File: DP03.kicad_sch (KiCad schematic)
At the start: 2 parts

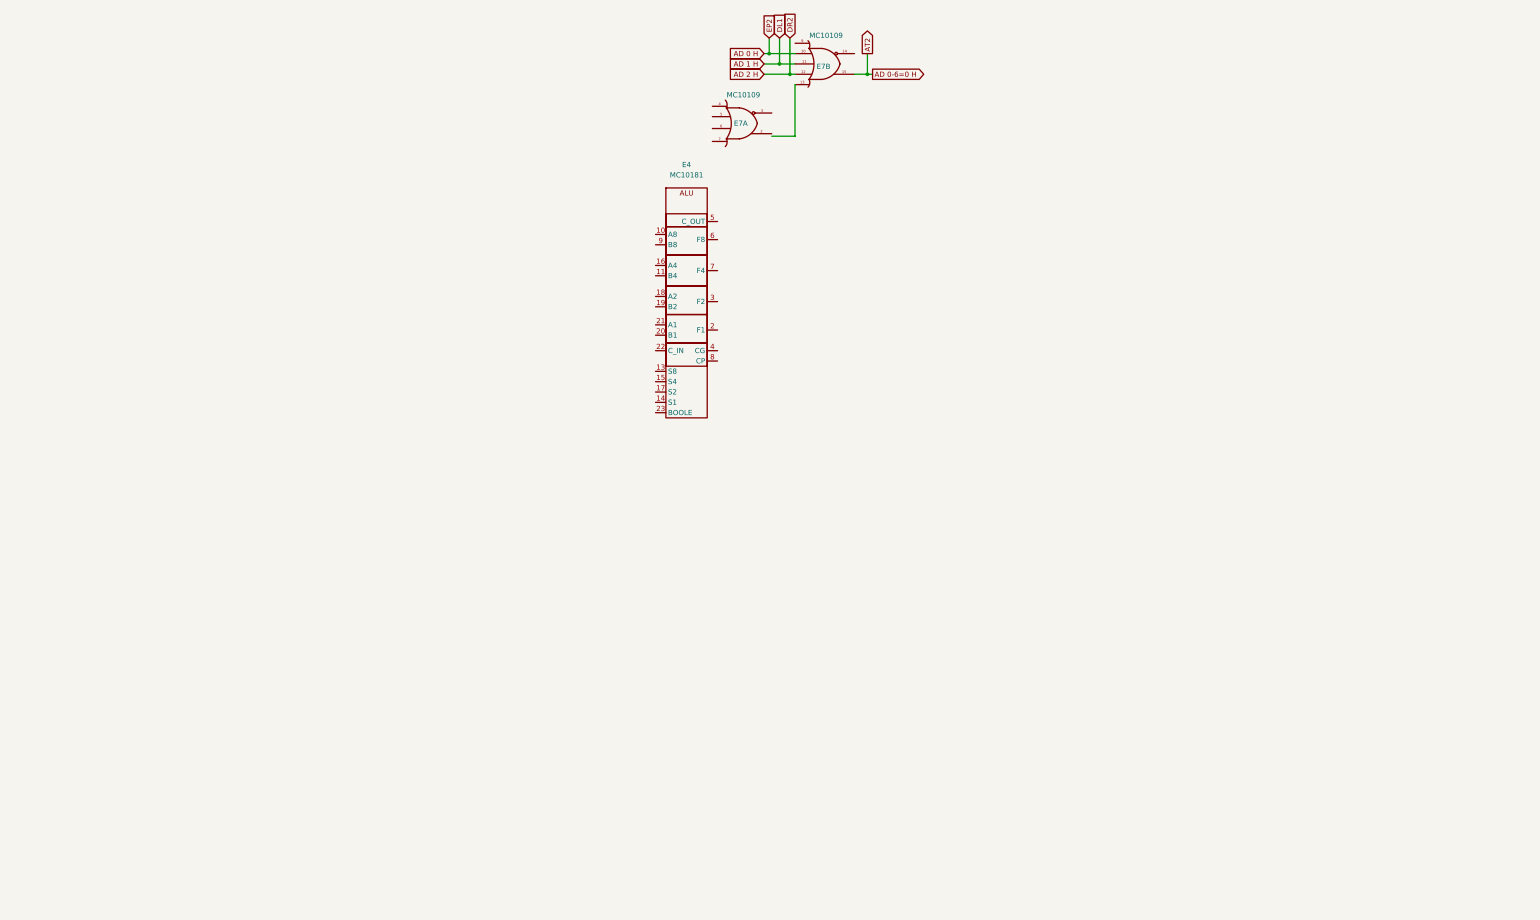
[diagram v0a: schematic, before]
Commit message: EDP is "done" but there is still much work to do to standardize and set up netlist export and verilog creation
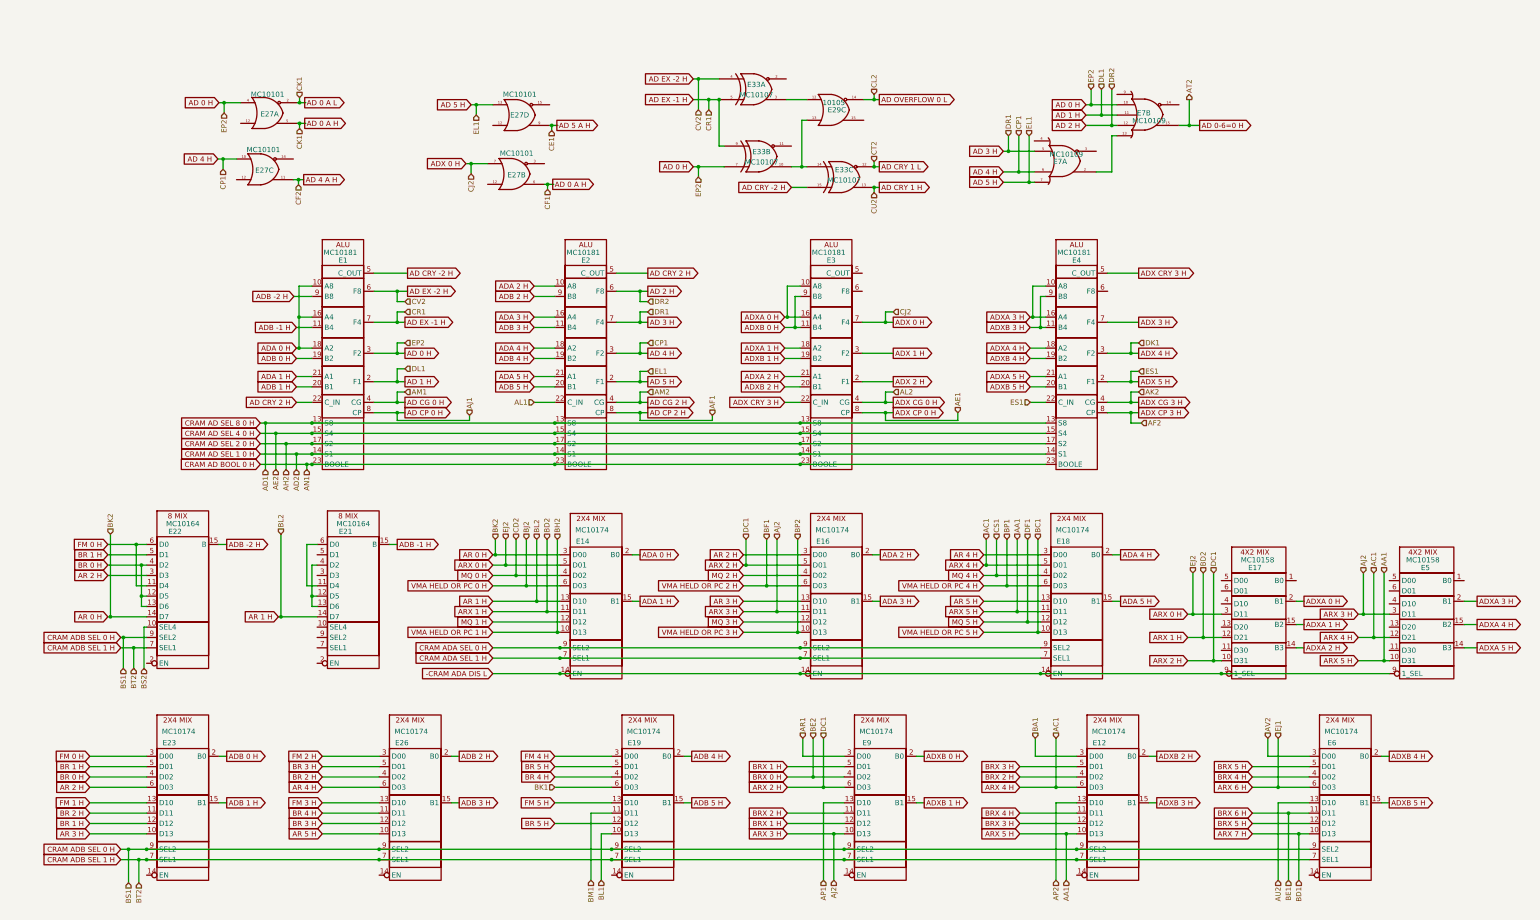
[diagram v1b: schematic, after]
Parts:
- added E1, E2, E3: MC10181, symbol DEC20:MC10181
- added E12, E14, E16, E18, E19, E23, E26, E6, E9: MC10174, symbol DEC20:MC10174
- added E17, E5: MC10158, symbol DEC20:MC10158
- added E21, E22: MC10164, symbol DEC20:MC10164
- added E27: MC10101, symbol DEC20:MC10101
- added E29: 10105, symbol DEC20:MC10105
- added E33: MC10107, symbol DEC20:MC10107
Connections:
- net AD 0 H: now also E1.3 (F2), E27.4 (Ain), E33.7 (Bin2)
- net AD 1 H: now also E1.2 (F1)
- net AD 2 H: now also E2.6 (F8)
- net GEE: now also E1.12 (GEE), E2.12 (GEE), E3.12 (GEE)
- net VCC1: now also E1.1 (VCC1), E12.1 (VCC1), E14.1 (VCC1), E16.1 (VCC1), E17.1 (VCC1), E18.1 (VCC1), E19.1 (VCC1), E2.1 (VCC1), E21.1 (VCC1), E22.1 (VCC1), E23.1 (VCC1), E26.1 (VCC1), E27.1 (VCC1), E27.1 (VCC1), E27.1 (VCC1), E27.1 (VCC1), E29.1 (VCC1), E3.1 (VCC1), E33.1 (VCC1), E33.1 (VCC1), E33.1 (VCC1), E5.1 (VCC1), E6.1 (VCC1), E9.1 (VCC1)
- net VCC2: now also E1.24 (VCC2), E12.16 (VCC2), E14.16 (VCC2), E16.16 (VCC2), E17.16 (VCC2), E18.16 (VCC2), E19.16 (VCC2), E2.24 (VCC2), E21.16 (VCC2), E22.16 (VCC2), E23.16 (VCC2), E26.16 (VCC2), E27.16 (VCC2), E27.16 (VCC2), E27.16 (VCC2), E27.16 (VCC2), E29.16 (VCC2), E3.24 (VCC2), E33.16 (VCC2), E33.16 (VCC2), E33.16 (VCC2), E5.16 (VCC2), E6.16 (VCC2), E9.16 (VCC2)
- net ADXA 3 H: now reaches E4.10 (A8)
- net ADXA 3 H: now also E4.16 (A4), E5.2 (B1)
- net ADXB 3 H: now reaches E4.11 (B4)
- net ADXB 3 H: now also E4.9 (B8), E12.15 (B1)
- net CRAM AD SEL 8 0 H: now reaches E4.13 (S8)
- net CRAM AD SEL 8 0 H: now also E1.13 (S8), E2.13 (S8), E3.13 (S8)
- net CRAM AD SEL 1 0 H: now reaches E4.14 (S1)
- net CRAM AD SEL 1 0 H: now also E1.14 (S1), E2.14 (S1), E3.14 (S1)
- net CRAM AD SEL 4 0 H: now reaches E4.15 (S4)
- net CRAM AD SEL 4 0 H: now also E1.15 (S4), E2.15 (S4), E3.15 (S4)
- net CRAM AD SEL 2 0 H: now reaches E4.17 (S2)
- net CRAM AD SEL 2 0 H: now also E1.17 (S2), E2.17 (S2), E3.17 (S2)
- net ADXA 4 H: now reaches E4.18 (A2)
- net ADXA 4 H: now also E5.15 (B2)
- net ADXB 4 H: now reaches E4.19 (B2)
- net ADXB 4 H: now also E6.2 (B0)
- net ADX 5 H: now reaches E4.2 (F1)
- net ADX 5 H: now also E4.22 (C_IN)
- net ADXB 5 H: now reaches E4.20 (B1)
- net ADXB 5 H: now also E6.15 (B1)
- net ADXA 5 H: now reaches E4.21 (A1)
- net ADXA 5 H: now also E5.14 (B3)
- net CRAM AD BOOL 0 H: now reaches E4.23 (BOOLE)
- net CRAM AD BOOL 0 H: now also E1.23 (BOOLE), E2.23 (BOOLE), E3.23 (BOOLE)
- net ADX 4 H: now reaches E4.3 (F2)
- net ADX CG 3 H: now reaches E4.4 (CG)
- net ADX CRY 3 H: now reaches E4.5 (C_OUT)
- net ADX CRY 3 H: now also E3.22 (C_IN)
- net ADX 3 H: now reaches E4.7 (F4)
- net ADX CP 3 H: now reaches E4.8 (CP)
- net at E7.2 (Aout): now also E7.13 (Bin5)
- net AD 3 H: now reaches E7.5 (Bin2)
- net AD 3 H: now also E2.7 (F4)
- net AD 4 H: now reaches E7.6 (Bin3)
- net AD 4 H: now also E2.3 (F2), E27.10 (Cin)
- net AD 5 H: now reaches E7.7 (Bin4)
- net AD 5 H: now also E2.2 (F1), E27.13 (Din)
- new net: E29.12 (Cin1), E33.3 (Aout)
- new net: E29.13 (Cin2), E33.10 (Bout), E33.14 (Cin1)
- new net: E21.11 (D4), E21.6 (D0)
- new net: E21.12 (D5), E21.13 (D6), E21.4 (D2)
- new net -CRAM ADA DIS L: E14.14 (EN), E16.14 (EN), E17.9 (1_SEL), E18.14 (EN), E5.9 (1_SEL)
- new net AD 0 A H: E27.2 (~Aout), E27.5 (Aout), E27.6 (Bout)
- new net AD 4 A H: E27.11 (Cout)
- new net AD 5 A H: E27.9 (Dout)
- new net AD CG 0 H: E1.4 (CG)
- new net AD CG 2 H: E2.4 (CG)
- new net AD CP 0 H: E1.8 (CP)
- new net AD CP 2 H: E2.8 (CP)
- new net AD CRY -2 H: E1.5 (C_OUT), E33.15 (Cin2)
- new net AD CRY 1 H: E33.13 (Cout)
- new net AD CRY 1 L: E33.12 (~Cout)
- new net AD CRY 2 H: E1.22 (C_IN), E2.5 (C_OUT)
- new net AD EX -1 H: E1.7 (F4), E33.5 (Ain2), E33.9 (Bin1)
- new net AD EX -2 H: E1.6 (F8), E33.4 (Ain1)
- new net AD OVERFLOW 0 L: E29.14 (~Cout)
- new net ADA 0 H: E1.10 (A8), E1.16 (A4), E1.18 (A2), E14.2 (B0)
- new net ADA 1 H: E1.21 (A1), E14.15 (B1)
- new net ADA 2 H: E16.2 (B0), E2.10 (A8)
- new net ADA 3 H: E16.15 (B1), E2.16 (A4)
- new net ADA 4 H: E18.2 (B0), E2.18 (A2)
- new net ADA 5 H: E18.15 (B1), E2.21 (A1)
- new net ADB -1 H: E1.11 (B4), E21.15 (B)
- new net ADB -2 H: E1.9 (B8), E22.15 (B)
- new net ADB 0 H: E1.19 (B2), E23.2 (B0)
- new net ADB 1 H: E1.20 (B1), E23.15 (B1)
- new net ADB 2 H: E2.9 (B8), E26.2 (B0)
- new net ADB 3 H: E2.11 (B4), E26.15 (B1)
- new net ADB 4 H: E19.2 (B0), E2.19 (B2)
- new net ADB 5 H: E19.15 (B1), E2.20 (B1)
- new net ADX 0 H: E27.7 (Bin), E3.7 (F4)
- new net ADX 1 H: E3.3 (F2)
- new net ADX 2 H: E3.2 (F1)
- new net ADX CG 0 H: E3.4 (CG)
- new net ADX CP 0 H: E3.8 (CP)
- new net ADXA 0 H: E17.2 (B1), E3.10 (A8), E3.16 (A4)
- new net ADXA 1 H: E17.15 (B2), E3.18 (A2)
- new net ADXA 2 H: E17.14 (B3), E3.21 (A1)
- new net ADXB 0 H: E3.11 (B4), E3.9 (B8), E9.2 (B0)
- new net ADXB 1 H: E3.19 (B2), E9.15 (B1)
- new net ADXB 2 H: E12.2 (B0), E3.20 (B1)
- new net AL1: E2.22 (C_IN)
- new net AP1: E9.13 (D10)
- new net AP2: E12.13 (D10)
- new net AR 0 H: E14.3 (D00), E22.14 (D7)
- new net AR 1 H: E14.13 (D10), E21.14 (D7)
- new net AR 2 H: E16.3 (D00), E22.3 (D3), E23.6 (D03)
- new net AR 3 H: E16.13 (D10), E23.10 (D13)
- new net AR 4 H: E18.3 (D00), E26.6 (D03)
- new net AR 5 H: E18.13 (D10), E26.10 (D13)
- new net AR1: E9.3 (D00)
- new net ARX 0 H: E14.5 (D01), E17.3 (D11)
- new net ARX 1 H: E14.11 (D11), E17.12 (D21)
- new net ARX 2 H: E16.5 (D01), E17.10 (D31), E9.6 (D03)
- new net ARX 3 H: E16.11 (D11), E5.3 (D11), E9.10 (D13)
- new net ARX 4 H: E12.6 (D03), E18.5 (D01), E5.12 (D21)
- new net ARX 5 H: E12.10 (D13), E18.11 (D11), E5.10 (D31)
- new net ARX 6 H: E6.6 (D03)
- new net ARX 7 H: E6.10 (D13)
- new net AU2: E6.13 (D10)
- new net AV2: E6.3 (D00)
- new net BA1: E12.3 (D00)
- new net BK1: E19.6 (D03)
- new net BL1: E19.10 (D13)
- new net BM1: E19.11 (D11)
- new net BR 0 H: E22.12 (D5), E22.13 (D6), E22.4 (D2), E23.4 (D02)
- new net BR 1 H: E22.5 (D1), E23.12 (D12), E23.5 (D01)
- new net BR 2 H: E23.11 (D11), E26.4 (D02)
- new net BR 3 H: E26.12 (D12), E26.5 (D01)
- new net BR 4 H: E19.4 (D02), E26.11 (D11)
- new net BR 5 H: E19.12 (D12), E19.5 (D01)
- new net BRX 0 H: E9.4 (D02)
- new net BRX 1 H: E9.12 (D12), E9.5 (D01)
- new net BRX 2 H: E12.4 (D02), E9.11 (D11)
- new net BRX 3 H: E12.12 (D12), E12.5 (D01)
- new net BRX 4 H: E12.11 (D11), E6.4 (D02)
- new net BRX 5 H: E6.12 (D12), E6.5 (D01)
- new net BRX 6 H: E6.11 (D11)
- new net BS2: E22.10 (SEL4)
- new net CRAM ADA SEL 0 H: E14.9 (SEL2), E16.9 (SEL2), E18.9 (SEL2)
- new net CRAM ADA SEL 1 H: E14.7 (SEL1), E16.7 (SEL1), E18.7 (SEL1)
- new net CRAM ADB SEL 0 H: E12.9 (SEL2), E19.9 (SEL2), E22.9 (SEL2), E23.9 (SEL2), E26.9 (SEL2), E6.9 (SEL2), E9.9 (SEL2)
- new net CRAM ADB SEL 1 H: E12.7 (SEL1), E19.7 (SEL1), E22.7 (SEL1), E23.7 (SEL1), E26.7 (SEL1), E6.7 (SEL1), E9.7 (SEL1)
- new net FM 0 H: E22.11 (D4), E22.6 (D0), E23.3 (D00)
- new net FM 1 H: E23.13 (D10)
- new net FM 2 H: E26.3 (D00)
- new net FM 3 H: E26.13 (D10)
- new net FM 4 H: E19.3 (D00)
- new net FM 5 H: E19.13 (D10)
- new net MQ 0 H: E14.4 (D02)
- new net MQ 1 H: E14.12 (D12)
- new net MQ 2 H: E16.4 (D02)
- new net MQ 3 H: E16.12 (D12)
- new net MQ 4 H: E18.4 (D02)
- new net MQ 5 H: E18.12 (D12)
- new net VEE: E12.8 (VEE), E14.8 (VEE), E16.8 (VEE), E17.8 (VEE), E18.8 (VEE), E19.8 (VEE), E21.8 (VEE), E22.8 (VEE), E23.8 (VEE), E26.8 (VEE), E5.8 (VEE), E6.8 (VEE), E9.8 (VEE)
- new net VMA HELD OR PC 0 H: E14.6 (D03)
- new net VMA HELD OR PC 1 H: E14.10 (D13)
- new net VMA HELD OR PC 2 H: E16.6 (D03)
- new net VMA HELD OR PC 3 H: E16.10 (D13)
- new net VMA HELD OR PC 4 H: E18.6 (D03)
- new net VMA HELD OR PC 5 H: E18.10 (D13)
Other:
- company: (none) -> DIGITAL
- title: (none) -> DATA PATH AD & ADX ADDERS
- moved on the sheet: E4, E7B

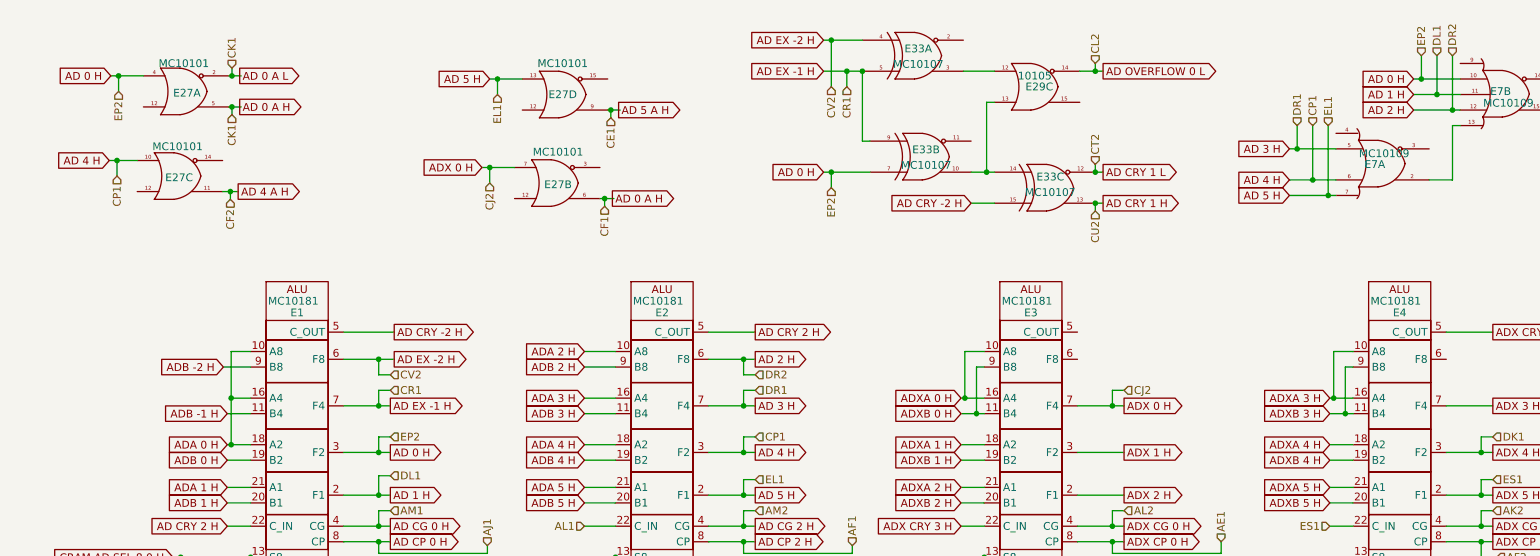
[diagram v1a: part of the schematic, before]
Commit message: Adding backplane connector slowly and painfully
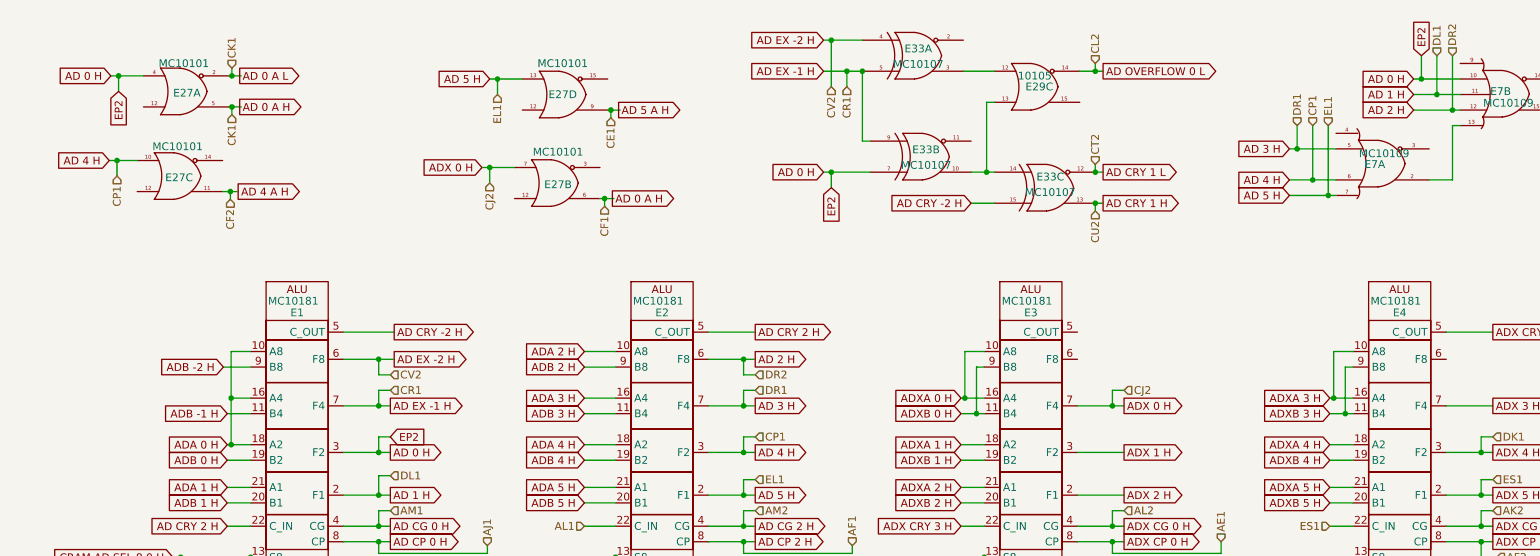
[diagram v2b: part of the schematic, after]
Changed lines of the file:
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@@
+    )
+  )
+  (global_label "EP2" (shape input) (at 143.51 93.345 0) (fields_autoplaced)
+    (effects (font (size 1.27 1.27)) (justify left))
+    (property "Intersheet References" "${INTERSHEET_REFS}" (id 0) (at 149.5517 93.2656 0)
+      (effects (font (size 1.27 1.27)) (justify left) hide)
     )
   )
@@
     )
   )
+  (global_label "EP2" (shape input) (at 215.646 52.578 270) (fields_autoplaced)
+    (effects (font (size 1.27 1.27)) (justify right))
+    (property "Intersheet References" "${INTERSHEET_REFS}" (id 0) (at 215.5666 58.6197 90)
+      (effects (font (size 1.27 1.27)) (justify right) hide)
+    )
+  )
   (global_label "ARX 3 H" (shape input) (at 226.695 159.385 180) (fields_autoplaced)
     (effects (font (size 1.27 1.27)) (justify right))
@@
     )
   )
+  (global_label "EP2" (shape input) (at 312.166 30.988 90) (fields_autoplaced)
+    (effects (font (size 1.27 1.27)) (justify left))
+    (property "Intersheet References" "${INTERSHEET_REFS}" (id 0) (at 312.0866 24.9463 90)
+      (effects (font (size 1.27 1.27)) (justify left) hide)
+    )
+  )
   (global_label "AR 2 H" (shape input) (at 70.485 150.495 180) (fields_autoplaced)
     (effects (font (size 1.27 1.27)) (justify right))
@@
     )
   )
+  (global_label "EP2" (shape input) (at 99.06 36.83 270) (fields_autoplaced)
+    (effects (font (size 1.27 1.27)) (justify right))
+    (property "Intersheet References" "${INTERSHEET_REFS}" (id 0) (at 98.9806 42.8717 90)
+      (effects (font (size 1.27 1.27)) (justify right) hide)
+    )
+  )
   (global_label "AD 5 H" (shape output) (at 203.2 102.87 0) (fields_autoplaced)
     (effects (font (size 1.27 1.27)) (justify left))
@@
     (effects (font (size 1.27 1.27)) (justify left))
   )
-  (hierarchical_label "EP2" (shape input) (at 312.166 30.988 90)
-    (effects (font (size 1.27 1.27)) (justify left))
-  )
   (hierarchical_label "CF1" (shape input) (at 178.562 55.626 270)
     (effects (font (size 1.27 1.27)) (justify right))
@@
     (effects (font (size 1.27 1.27)) (justify left))
   )
-  (hierarchical_label "EP2" (shape input) (at 143.51 93.345 0)
-    (effects (font (size 1.27 1.27)) (justify left))
-  )
   (hierarchical_label "AN1" (shape input) (at 119.38 124.46 270)
     (effects (font (size 1.27 1.27)) (justify right))
@@
     (effects (font (size 1.27 1.27)) (justify left))
   )
-  (hierarchical_label "EP2" (shape input) (at 99.06 36.83 270)
-    (effects (font (size 1.27 1.27)) (justify right))
-  )
   (hierarchical_label "CK1" (shape input) (at 117.602 40.64 270)
     (effects (font (size 1.27 1.27)) (justify right))
@@
     (effects (font (size 1.27 1.27)) (justify left))
   )
-  (hierarchical_label "EP2" (shape input) (at 215.646 52.578 270)
-    (effects (font (size 1.27 1.27)) (justify right))
-  )
   (hierarchical_label "DK1" (shape input) (at 323.85 93.345 0)
